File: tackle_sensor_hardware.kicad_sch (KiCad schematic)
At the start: 82 parts, among them J1 Conn_01x02_Male, J2 Conn_01x04_Male, J3 Conn_01x03_Male, J4 Conn_ARM_JTAG_SWD_10, Q1 DMP4051LK3, Q2 2N7002K, Q3 2N7002K, Q4 2N7002K, Q5 2N7002K, Q6 2N7002K, Q7 2N7002K, Q9 CSD19538Q3A, SW1 SW_Push, SW2 SW_DIP_x01, T1 DRQ125-330-R, U1 LIS2DE12, U2 STM32G031Fx, U3 LM3488, U4 LD1117S33TR_SOT223, U5 NIS5420MT6TXG

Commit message: routing in progress.
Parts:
- C6, C7: footprint (none) -> Capacitor_SMD:C_0402_1005Metric
- R3: footprint Resistor_SMD:R_0603_1608Metric -> Resistor_SMD:R_0402_1005Metric
- gave numbers to parts that had none: 2
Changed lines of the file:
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@@
   (symbol (lib_id "Device:R_US") (at 274.32 142.24 180) (unit 1)
     (in_bom yes) (on_board yes) (fields_autoplaced)
-    (property "Reference" "R?" (id 0) (at 276.86 140.9699 0)
+    (property "Reference" "R18" (id 0) (at 276.86 140.9699 0)
       (effects (font (size 1.27 1.27)) (justify right))
     )
@@
       (effects (font (size 1.27 1.27)) (justify left))
     )
-    (property "Footprint" "" (id 2) (at 106.3752 92.71 0)
+    (property "Footprint" "Capacitor_SMD:C_0402_1005Metric" (id 2) (at 106.3752 92.71 0)
       (effects (font (size 1.27 1.27)) hide)
     )
@@
       (effects (font (size 1.27 1.27)) (justify left))
     )
-    (property "Footprint" "Resistor_SMD:R_0603_1608Metric" (id 2) (at 106.426 81.534 90)
+    (property "Footprint" "Resistor_SMD:R_0402_1005Metric" (id 2) (at 106.426 81.534 90)
       (effects (font (size 1.27 1.27)) hide)
     )
@@
       (effects (font (size 1.27 1.27)) (justify left))
     )
-    (property "Footprint" "" (id 2) (at 93.6752 87.63 0)
+    (property "Footprint" "Capacitor_SMD:C_0402_1005Metric" (id 2) (at 93.6752 87.63 0)
       (effects (font (size 1.27 1.27)) hide)
     )
@@
   (symbol (lib_id "Device:R_US") (at 298.45 142.24 180) (unit 1)
     (in_bom yes) (on_board yes) (fields_autoplaced)
-    (property "Reference" "R?" (id 0) (at 300.99 140.9699 0)
+    (property "Reference" "R20" (id 0) (at 300.99 140.9699 0)
       (effects (font (size 1.27 1.27)) (justify right))
     )
@@
     )
     (path "/84b2e8c0-f17e-4c6f-9a69-984374f700ab"
-      (reference "C6") (unit 1) (value "C") (footprint "")
+      (reference "C6") (unit 1) (value "C") (footprint "Capacitor_SMD:C_0402_1005Metric")
     )
     (path "/43efc653-c82a-45e7-8b5f-a91e903fb8c8"
-      (reference "C7") (unit 1) (value "C") (footprint "")
+      (reference "C7") (unit 1) (value "C") (footprint "Capacitor_SMD:C_0402_1005Metric")
     )
     (path "/109a1cc3-2724-4e09-bfdd-2cd7cc22195e"
@@
     )
     (path "/776bfe19-e581-4d73-80c0-1958bddf5275"
-      (reference "R3") (unit 1) (value "R_US") (footprint "Resistor_SMD:R_0603_1608Metric")
+      (reference "R3") (unit 1) (value "R_US") (footprint "Resistor_SMD:R_0402_1005Metric")
     )
     (path "/2dec3f16-d443-4e35-ae47-c02c1ae03a32"
@@
       (reference "R17") (unit 1) (value "10k,1%,63mW") (footprint "Resistor_SMD:R_0402_1005Metric")
     )
+    (path "/055c3ea3-2f19-4ca3-9331-60b0bf245082"
+      (reference "R18") (unit 1) (value "0,0.5W") (footprint "Resistor_SMD:R_1210_3225Metric")
+    )
     (path "/de7f81a9-0eb0-4003-9006-42bfb2a46e67"
       (reference "R19") (unit 1) (value "1k,1%,25mW") (footprint "Resistor_SMD:R_0603_1608Metric")
     )
+    (path "/bdc19a75-08f9-4db4-88b6-1fb78b7b83c0"
+      (reference "R20") (unit 1) (value "0,0.5W") (footprint "Resistor_SMD:R_1210_3225Metric")
+    )
     (path "/cc817cae-5b9c-433c-a042-7a7f554ec91c"
       (reference "R21") (unit 1) (value "220,1%,63mW") (footprint "Resistor_SMD:R_0402_1005Metric")
@@
       (reference "R26") (unit 1) (value "1k") (footprint "Resistor_SMD:R_0603_1608Metric")
     )
-    (path "/055c3ea3-2f19-4ca3-9331-60b0bf245082"
-      (reference "R?") (unit 1) (value "0,0.5W") (footprint "Resistor_SMD:R_1210_3225Metric")
-    )
-    (path "/bdc19a75-08f9-4db4-88b6-1fb78b7b83c0"
-      (reference "R?") (unit 1) (value "0,0.5W") (footprint "Resistor_SMD:R_1210_3225Metric")
-    )
     (path "/35867e80-c0f2-4b27-b083-3610a422bd27"

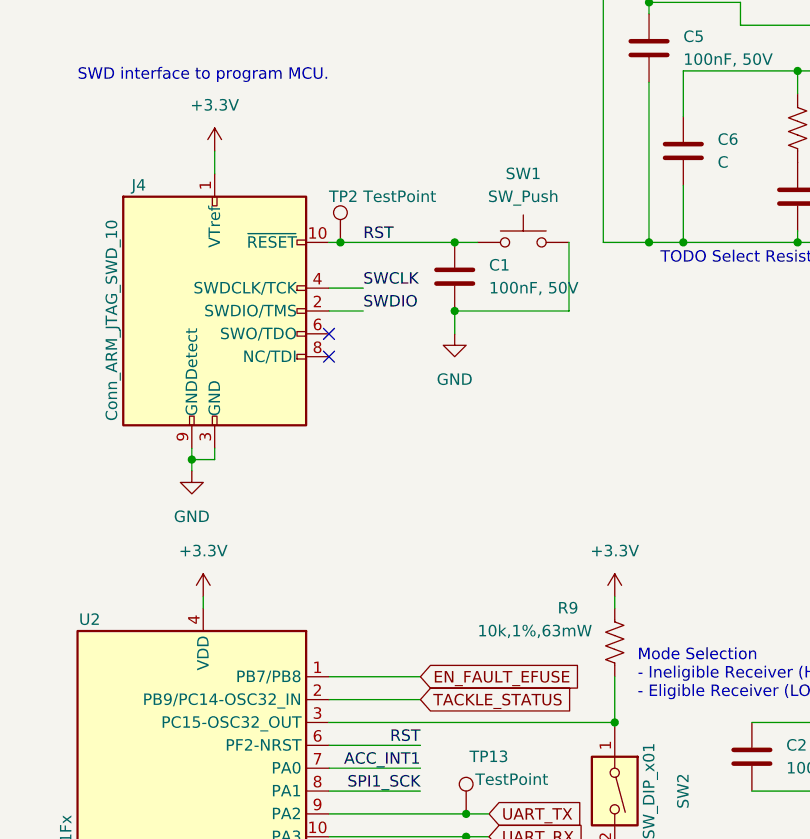
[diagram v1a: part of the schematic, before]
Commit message: update reset button, add decoupling caps for MCU.
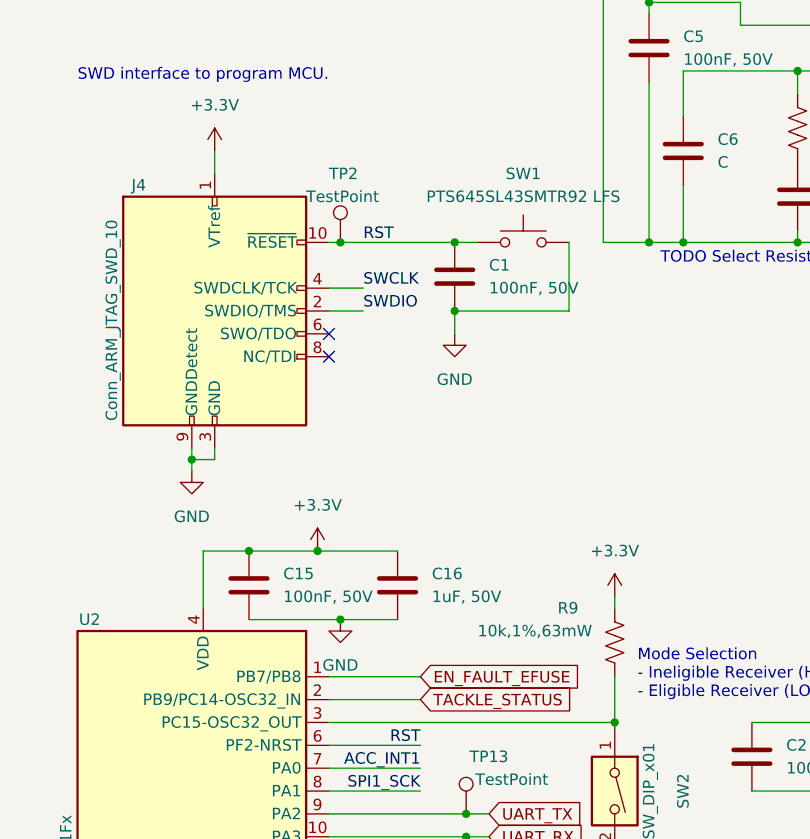
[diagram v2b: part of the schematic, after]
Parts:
- added C15: 100nF, 50V, Capacitor_SMD:C_0805_2012Metric, symbol Device:C
- added C16: 1uF, 50V, Capacitor_SMD:C_0603_1608Metric, symbol Device:C
- SW1: value SW_Push -> PTS645SL43SMTR92 LFS; footprint Resistor_SMD:R_1210_3225Metric -> Button_Switch_SMD:SW_SPST_PTS645
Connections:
- net +3V3: now also C15.1, C16.1
- net GND: now also C15.2, C16.2
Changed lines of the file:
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@@
   (junction (at 127 93.98) (diameter 0) (color 0 0 0 0)
   )
+  (junction (at 44.45 128.27) (diameter 0) (color 0 0 0 0)
+  )
   (junction (at 123.19 154.94) (diameter 0) (color 0 0 0 0)
   )
@@
   (junction (at 254 45.72) (diameter 0) (color 0 0 0 0)
   )
+  (junction (at 52.07 128.27) (diameter 0) (color 0 0 0 0)
+  )
   (junction (at 116.84 154.94) (diameter 0) (color 0 0 0 0)
   )
@@
   (junction (at 58.42 35.56) (diameter 0) (color 0 0 0 0)
   )
+  (junction (at 54.61 135.89) (diameter 0) (color 0 0 0 0)
+  )
   (junction (at 203.2 45.72) (diameter 0) (color 0 0 0 0)
   )
@@
     (stroke (width 0) (type default) (color 0 0 0 0))
   )
+  (wire (pts (xy 44.45 128.27) (xy 52.07 128.27))
+    (stroke (width 0) (type default) (color 0 0 0 0))
+  )
   (wire (pts (xy 88.9 35.56) (xy 88.9 67.31))
     (stroke (width 0) (type default) (color 0 0 0 0))
@@
     (stroke (width 0) (type default) (color 0 0 0 0))
   )
+  (wire (pts (xy 54.61 135.89) (xy 60.96 135.89))
+    (stroke (width 0) (type default) (color 0 0 0 0))
+  )
   (wire (pts (xy 246.38 133.35) (xy 246.38 135.89))
     (stroke (width 0) (type default) (color 0 0 0 0))
@@
     (stroke (width 0) (type default) (color 0 0 0 0))
   )
-  (wire (pts (xy 80.01 93.98) (xy 80.01 101.6))
-    (stroke (width 0) (type default) (color 0 0 0 0))
-  )
   (wire (pts (xy 53.34 180.34) (xy 63.5 180.34))
     (stroke (width 0) (type default) (color 0 0 0 0))
@@
     (stroke (width 0) (type default) (color 0 0 0 0))
   )
+  (wire (pts (xy 44.45 128.27) (xy 39.37 128.27))
+    (stroke (width 0) (type default) (color 0 0 0 0))
+  )
   (wire (pts (xy 228.6 130.81) (xy 228.6 133.35))
     (stroke (width 0) (type default) (color 0 0 0 0))
@@
     (stroke (width 0) (type default) (color 0 0 0 0))
   )
-  (wire (pts (xy 39.37 133.35) (xy 39.37 134.62))
+  (wire (pts (xy 39.37 128.27) (xy 39.37 134.62))
     (stroke (width 0) (type default) (color 0 0 0 0))
   )
@@
     (stroke (width 0) (type default) (color 0 0 0 0))
   )
+  (wire (pts (xy 80.01 93.98) (xy 80.01 101.6))
+    (stroke (width 0) (type default) (color 0 0 0 0))
+  )
   (wire (pts (xy 243.84 58.42) (xy 237.49 58.42))
     (stroke (width 0) (type default) (color 0 0 0 0))
@@
     (stroke (width 0) (type default) (color 0 0 0 0))
   )
+  (wire (pts (xy 44.45 135.89) (xy 54.61 135.89))
+    (stroke (width 0) (type default) (color 0 0 0 0))
+  )
   (wire (pts (xy 318.77 106.68) (xy 318.77 109.22))
     (stroke (width 0) (type default) (color 0 0 0 0))
@@
     (stroke (width 0) (type default) (color 0 0 0 0))
   )
+  (wire (pts (xy 52.07 128.27) (xy 60.96 128.27))
+    (stroke (width 0) (type default) (color 0 0 0 0))
+  )
   (wire (pts (xy 237.49 147.32) (xy 237.49 152.4))
     (stroke (width 0) (type default) (color 0 0 0 0))
@@
     (pin "2")
   )
-  (symbol (lib_id "Switch:SW_Push") (at 74.93 93.98 0) (unit 1)
-    (in_bom yes) (on_board yes) (fields_autoplaced)
-    (property "Reference" "SW1" (id 0) (at 74.93 86.36 0))
-    (property "Value" "SW_Push" (id 1) (at 74.93 88.9 0))
-    (property "Footprint" "Resistor_SMD:R_1210_3225Metric" (id 2) (at 74.93 88.9 0)
-      (effects (font (size 1.27 1.27)) hide)
-    )
-    (property "Datasheet" "~" (id 3) (at 74.93 88.9 0)
-      (effects (font (size 1.27 1.27)) hide)
-    )
-    (pin "1")
-    (pin "2")
-  )
   (symbol (lib_id "Transistor_FET:2N7002K") (at 198.12 152.4 0) (unit 1)
     (in_bom yes) (on_board yes)
@@
     (pin "1")
   )
+  (symbol (lib_id "Device:C") (at 44.45 132.08 0) (unit 1)
+    (in_bom yes) (on_board yes) (fields_autoplaced)
+    (property "Reference" "C15" (id 0) (at 48.26 130.8099 0)
+      (effects (font (size 1.27 1.27)) (justify left))
+    )
+    (property "Value" "100nF, 50V" (id 1) (at 48.26 133.3499 0)
+      (effects (font (size 1.27 1.27)) (justify left))
+    )
+    (property "Footprint" "Capacitor_SMD:C_0805_2012Metric" (id 2) (at 45.4152 135.89 0)
+      (effects (font (size 1.27 1.27)) hide)
+    )
+    (property "Datasheet" "https://www.yageo.com/upload/media/product/productsearch/datasheet/mlcc/UPY-GPHC_X7R_6.3V-to-50V_20.pdf" (id 3) (at 44.45 132.08 0)
+      (effects (font (size 1.27 1.27)) hide)
+    )
+    (property "MPN" "CC0805KRX7R9BB104" (id 4) (at 44.45 132.08 0)
+      (effects (font (size 1.27 1.27)) hide)
+    )
+    (pin "1")
+    (pin "2")
+  )
   (symbol (lib_id "Device:R_US") (at 264.16 157.48 0) (unit 1)
     (in_bom yes) (on_board yes)
@@
     (pin "9")
   )
+  (symbol (lib_id "power:GND") (at 54.61 135.89 0) (unit 1)
+    (in_bom yes) (on_board yes) (fields_autoplaced)
+    (property "Reference" "#PWR0129" (id 0) (at 54.61 142.24 0)
+      (effects (font (size 1.27 1.27)) hide)
+    )
+    (property "Value" "GND" (id 1) (at 54.61 140.97 0))
+    (property "Footprint" "" (id 2) (at 54.61 135.89 0)
+      (effects (font (size 1.27 1.27)) hide)
+    )
+    (property "Datasheet" "" (id 3) (at 54.61 135.89 0)
+      (effects (font (size 1.27 1.27)) hide)
+    )
+    (pin "1")
+  )
   (symbol (lib_id "power:+3.3V") (at 85.09 133.35 0) (unit 1)
     (in_bom yes) (on_board yes) (fields_autoplaced)
@@
   (symbol (lib_id "Connector:TestPoint") (at 54.61 93.98 0) (unit 1)
     (in_bom yes) (on_board yes)
-    (property "Reference" "TP2" (id 0) (at 53.34 88.9 0)
+    (property "Reference" "TP2" (id 0) (at 53.34 86.36 0)
       (effects (font (size 1.27 1.27)) (justify left))
     )
-    (property "Value" "TestPoint" (id 1) (at 57.15 88.9 0)
+    (property "Value" "TestPoint" (id 1) (at 50.8 88.9 0)
       (effects (font (size 1.27 1.27)) (justify left))
     )
@@
     (pin "1")
   )
+  (symbol (lib_id "Switch:SW_Push") (at 74.93 93.98 0) (unit 1)
+    (in_bom yes) (on_board yes) (fields_autoplaced)
+    (property "Reference" "SW1" (id 0) (at 74.93 86.36 0))
+    (property "Value" "PTS645SL43SMTR92 LFS" (id 1) (at 74.93 88.9 0))
+    (property "Footprint" "Button_Switch_SMD:SW_SPST_PTS645" (id 2) (at 74.93 88.9 0)
+      (effects (font (size 1.27 1.27)) hide)
+    )
+    (property "Datasheet" "https://www.ckswitches.com/media/1471/pts645.pdf" (id 3) (at 74.93 88.9 0)
+      (effects (font (size 1.27 1.27)) hide)
+    )
+    (pin "1")
+    (pin "2")
+  )
   (symbol (lib_id "Transistor_FET:2N7002K") (at 295.91 152.4 0) (unit 1)
     (in_bom yes) (on_board yes)
@@
     (pin "3")
   )
+  (symbol (lib_id "Device:C") (at 60.96 132.08 0) (unit 1)
+    (in_bom yes) (on_board yes) (fields_autoplaced)
+    (property "Reference" "C16" (id 0) (at 64.77 130.8099 0)
+      (effects (font (size 1.27 1.27)) (justify left))
+    )
+    (property "Value" "1uF, 50V" (id 1) (at 64.77 133.3499 0)
+      (effects (font (size 1.27 1.27)) (justify left))
+    )
+    (property "Footprint" "Capacitor_SMD:C_0603_1608Metric" (id 2) (at 61.9252 135.89 0)
+      (effects (font (size 1.27 1.27)) hide)
+    )
+    (property "Datasheet" "https://product.tdk.com/system/files/dam/doc/product/capacitor/ceramic/mlcc/catalog/mlcc_commercial_general_en.pdf" (id 3) (at 60.96 132.08 0)
+      (effects (font (size 1.27 1.27)) hide)
+    )
+    (property "MPN" "C1608X5R1H105K080AB" (id 4) (at 60.96 132.08 90)
+      (effects (font (size 1.27 1.27)) hide)
+    )
+    (pin "1")
+    (pin "2")
+  )
   (symbol (lib_id "Device:R_US") (at 200.66 139.7 0) (unit 1)
     (in_bom yes) (on_board yes) (fields_autoplaced)
@@
     (pin "1")
   )
-  (symbol (lib_id "power:+3.3V") (at 39.37 133.35 0) (unit 1)
+  (symbol (lib_id "power:+3.3V") (at 52.07 128.27 0) (unit 1)
     (in_bom yes) (on_board yes) (fields_autoplaced)
-    (property "Reference" "#PWR0104" (id 0) (at 39.37 137.16 0)
+    (property "Reference" "#PWR0104" (id 0) (at 52.07 132.08 0)
       (effects (font (size 1.27 1.27)) hide)
     )
-    (property "Value" "+3.3V" (id 1) (at 39.37 128.27 0))
-    (property "Footprint" "" (id 2) (at 39.37 133.35 0)
+    (property "Value" "+3.3V" (id 1) (at 52.07 123.19 0))
+    (property "Footprint" "" (id 2) (at 52.07 128.27 0)
       (effects (font (size 1.27 1.27)) hide)
     )
-    (property "Datasheet" "" (id 3) (at 39.37 133.35 0)
+    (property "Datasheet" "" (id 3) (at 52.07 128.27 0)
       (effects (font (size 1.27 1.27)) hide)
     )
@@
       (reference "#PWR0128") (unit 1) (value "+12V") (footprint "")
     )
+    (path "/7f02b77a-669b-4c09-8a20-21554f588e21"
+      (reference "#PWR0129") (unit 1) (value "GND") (footprint "")
+    )
     (path "/51d04bf7-7f46-44ad-aa72-25acae975c0f"
       (reference "C1") (unit 1) (value "100nF, 50V") (footprint "Capacitor_SMD:C_0805_2012Metric")
@@
       (reference "C14") (unit 1) (value "DNP") (footprint "Capacitor_SMD:C_0402_1005Metric")
     )
+    (path "/628ce136-c60f-4f6b-a1b9-780af9cab8b6"
+      (reference "C15") (unit 1) (value "100nF, 50V") (footprint "Capacitor_SMD:C_0805_2012Metric")
+    )
+    (path "/b5e3c22e-d373-459f-a3ce-4b8c26e51ce1"
+      (reference "C16") (unit 1) (value "1uF, 50V") (footprint "Capacitor_SMD:C_0603_1608Metric")
+    )
     (path "/c3e1c4c6-64d8-4eb6-86eb-759cbb00d7a2"
       (reference "D1") (unit 1) (value "SS2PH10HM3_A/H") (footprint "Diode_SMD:D_Powermite_AK")
@@
       (reference "R26") (unit 1) (value "1k") (footprint "Resistor_SMD:R_0603_1608Metric")
     )
-    (path "/35867e80-c0f2-4b27-b083-3610a422bd27"
-      (reference "SW1") (unit 1) (value "SW_Push") (footprint "Resistor_SMD:R_1210_3225Metric")
+    (path "/a8ac60ce-27be-4c48-9ae2-6ba0b7d265f6"
+      (reference "SW1") (unit 1) (value "PTS645SL43SMTR92 LFS") (footprint "Button_Switch_SMD:SW_SPST_PTS645")
     )
     (path "/e28615f2-7821-4d76-be46-f3030a98c4f0"

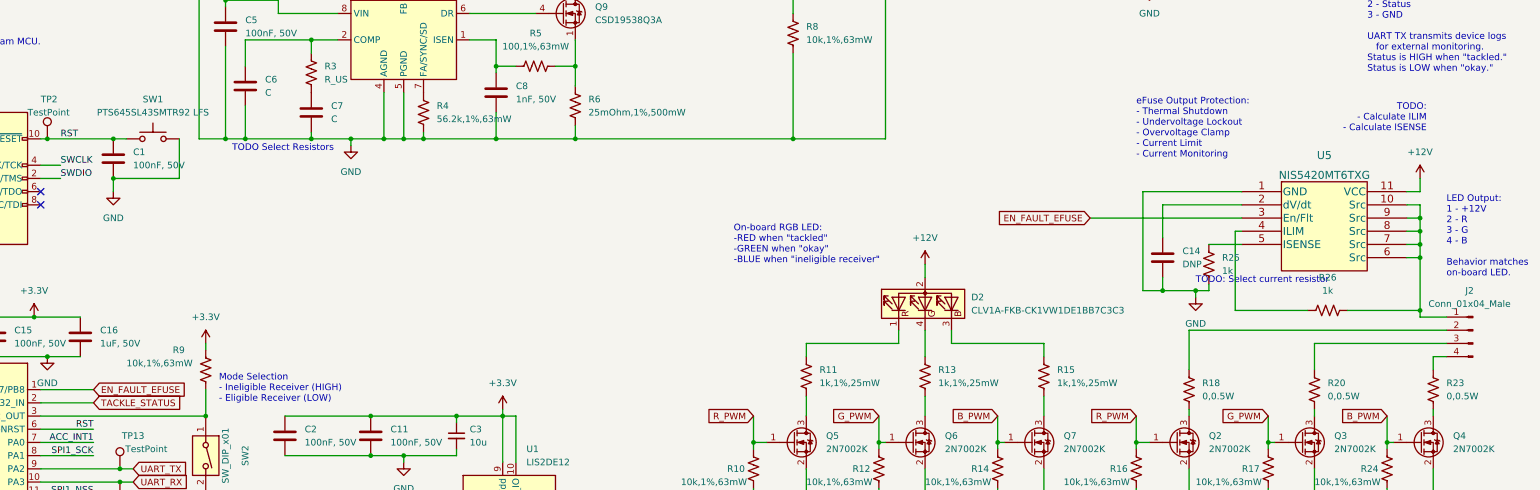
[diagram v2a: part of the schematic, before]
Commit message: added PTC
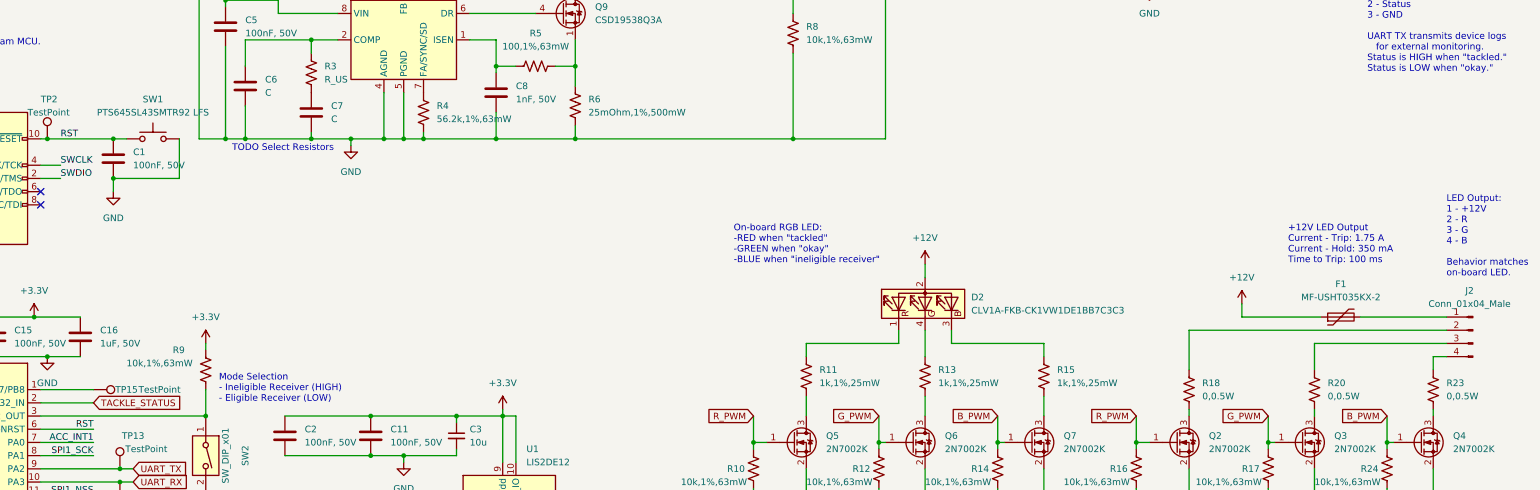
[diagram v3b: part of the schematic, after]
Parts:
- removed C14: DNP, Capacitor_SMD:C_0402_1005Metric, symbol Device:C
- removed R25, R26: 1k, Resistor_SMD:R_0603_1608Metric, symbol Device:R_US
- removed U5: NIS5420MT6TXG, rfc_footprint_lib:WDFN10_522AA-01_ONS, symbol rfc_symbol_lib:NIS5420MT6TXG
- added F1: MF-USHT035KX-2, Resistor_SMD:R_1210_3225Metric, symbol Device:Polyfuse
- added TP15: TestPoint, TestPoint:TestPoint_Pad_D1.5mm, symbol Connector:TestPoint
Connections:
- net +12V: now also F1.1
- net at J2.1 (Pin_1): now also F1.2
- net EN_FAULT_EFUSE: no longer names the net of U2.1 (PB7/PB8)
- net EN_FAULT_EFUSE: now also TP15.1
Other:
- note added: "+12V LED Output Current - Trip: 1.75 A Current - Hold: 350 mA Time to Trip: 100 ms"
- note removed: "TODO: - Calculate ILIM - Calculate ISENSE"
- note removed: "TODO: Select current resistor"
- note removed: "eFuse Output Protection: - Thermal Shutdown - Undervoltage Lockout - Overvoltage Clamp - Current Limit - Current Monitoring"
